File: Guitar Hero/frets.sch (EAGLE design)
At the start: 9 parts

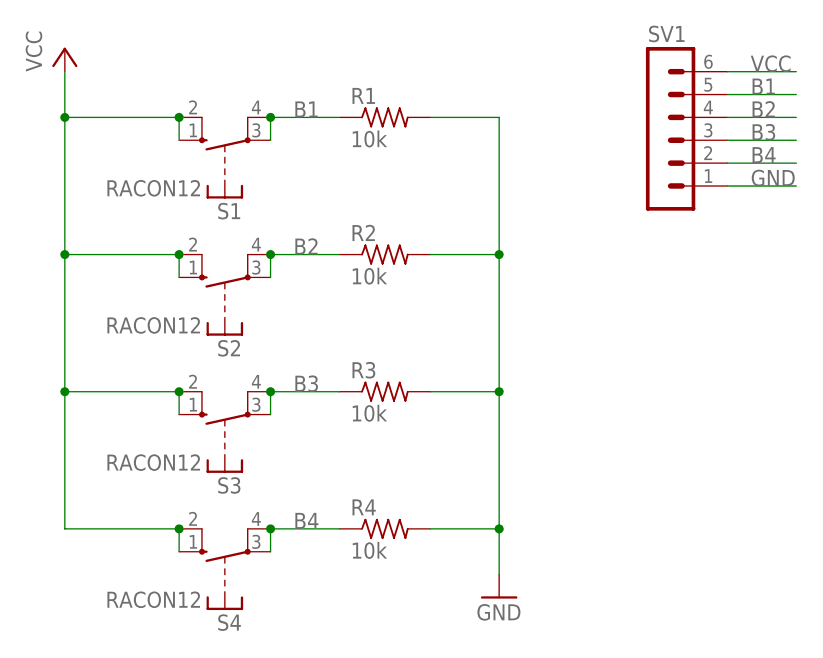
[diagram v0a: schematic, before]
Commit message: Started on base board; made board layout for peripherals
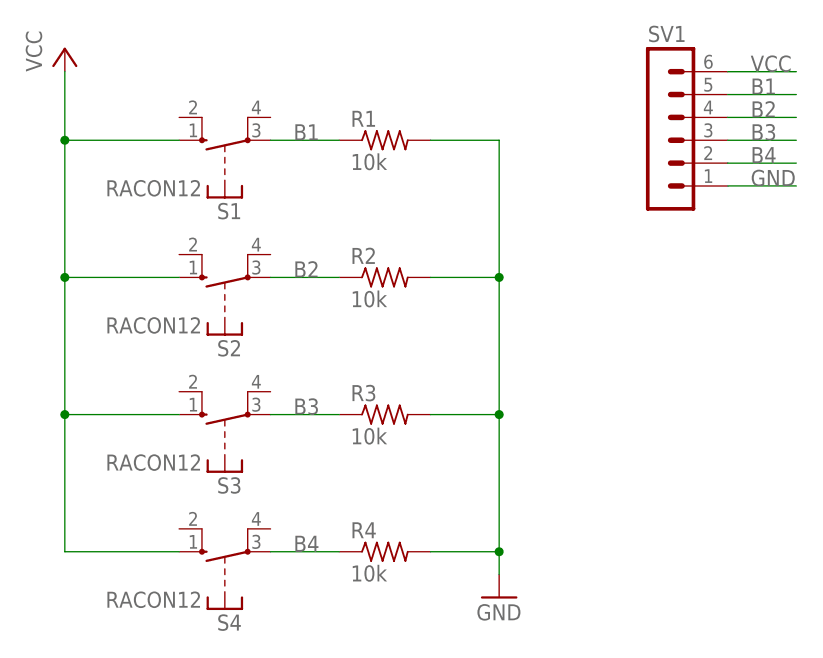
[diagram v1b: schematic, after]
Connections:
- net B1: no longer S1.P@1
- net B2: no longer S2.P@1
- net B3: no longer S3.P@1
- net B4: no longer S4.P@1
- net VCC: no longer S1.S@1, S2.S@1, S3.S@1, S4.S@1
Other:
- moved on the sheet: R1, R2, R3, R4
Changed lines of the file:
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@@
 </plain>
 <instances>
-<instance part="R1" gate="G$1" x="38.1" y="76.2"/>
-<instance part="R2" gate="G$1" x="38.1" y="60.96"/>
-<instance part="R3" gate="G$1" x="38.1" y="45.72"/>
-<instance part="R4" gate="G$1" x="38.1" y="30.48"/>
+<instance part="R1" gate="G$1" x="38.1" y="73.66"/>
+<instance part="R2" gate="G$1" x="38.1" y="58.42"/>
+<instance part="R3" gate="G$1" x="38.1" y="43.18"/>
+<instance part="R4" gate="G$1" x="38.1" y="27.94"/>
 <instance part="S1" gate="1" x="20.32" y="73.66" rot="R90"/>
 <instance part="S2" gate="1" x="20.32" y="58.42" rot="R90"/>
@@
 <net name="B1" class="0">
 <segment>
-<pinref part="S1" gate="1" pin="P@1"/>
 <pinref part="R1" gate="G$1" pin="1"/>
-<wire x1="25.4" y1="76.2" x2="33.02" y2="76.2" width="0.1524" layer="91"/>
-<label x="27.94" y="76.2" size="1.778" layer="95"/>
+<label x="27.94" y="73.66" size="1.778" layer="95"/>
 <pinref part="S1" gate="1" pin="P"/>
-<wire x1="25.4" y1="73.66" x2="25.4" y2="76.2" width="0.1524" layer="91"/>
-<junction x="25.4" y="76.2"/>
+<wire x1="25.4" y1="73.66" x2="33.02" y2="73.66" width="0.1524" layer="91"/>
 </segment>
 <segment>
@@
 <segment>
 <pinref part="R2" gate="G$1" pin="1"/>
-<pinref part="S2" gate="1" pin="P@1"/>
-<wire x1="33.02" y1="60.96" x2="25.4" y2="60.96" width="0.1524" layer="91"/>
-<label x="27.94" y="60.96" size="1.778" layer="95"/>
+<label x="27.94" y="58.42" size="1.778" layer="95"/>
 <pinref part="S2" gate="1" pin="P"/>
-<wire x1="25.4" y1="60.96" x2="25.4" y2="58.42" width="0.1524" layer="91"/>
-<junction x="25.4" y="60.96"/>
+<wire x1="33.02" y1="58.42" x2="25.4" y2="58.42" width="0.1524" layer="91"/>
 </segment>
 <segment>
@@
 <net name="B3" class="0">
 <segment>
-<pinref part="S3" gate="1" pin="P@1"/>
 <pinref part="R3" gate="G$1" pin="1"/>
-<wire x1="25.4" y1="45.72" x2="33.02" y2="45.72" width="0.1524" layer="91"/>
-<label x="27.94" y="45.72" size="1.778" layer="95"/>
+<label x="27.94" y="43.18" size="1.778" layer="95"/>
 <pinref part="S3" gate="1" pin="P"/>
-<wire x1="25.4" y1="43.18" x2="25.4" y2="45.72" width="0.1524" layer="91"/>
-<junction x="25.4" y="45.72"/>
+<wire x1="25.4" y1="43.18" x2="33.02" y2="43.18" width="0.1524" layer="91"/>
 </segment>
 <segment>
@@
 <net name="B4" class="0">
 <segment>
-<pinref part="S4" gate="1" pin="P@1"/>
 <pinref part="R4" gate="G$1" pin="1"/>
-<wire x1="25.4" y1="30.48" x2="33.02" y2="30.48" width="0.1524" layer="91"/>
-<label x="27.94" y="30.48" size="1.778" layer="95"/>
+<label x="27.94" y="27.94" size="1.778" layer="95"/>
 <pinref part="S4" gate="1" pin="P"/>
-<wire x1="25.4" y1="27.94" x2="25.4" y2="30.48" width="0.1524" layer="91"/>
-<junction x="25.4" y="30.48"/>
+<wire x1="33.02" y1="27.94" x2="25.4" y2="27.94" width="0.1524" layer="91"/>
 </segment>
 <segment>
@@
 <net name="VCC" class="0">
 <segment>
-<pinref part="S1" gate="1" pin="S@1"/>
-<wire x1="15.24" y1="76.2" x2="2.54" y2="76.2" width="0.1524" layer="91"/>
-<wire x1="2.54" y1="76.2" x2="2.54" y2="60.96" width="0.1524" layer="91"/>
-<pinref part="S4" gate="1" pin="S@1"/>
-<wire x1="2.54" y1="60.96" x2="2.54" y2="45.72" width="0.1524" layer="91"/>
-<wire x1="2.54" y1="45.72" x2="2.54" y2="30.48" width="0.1524" layer="91"/>
-<wire x1="2.54" y1="30.48" x2="15.24" y2="30.48" width="0.1524" layer="91"/>
-<pinref part="S3" gate="1" pin="S@1"/>
-<wire x1="15.24" y1="45.72" x2="2.54" y2="45.72" width="0.1524" layer="91"/>
-<junction x="2.54" y="45.72"/>
-<pinref part="S2" gate="1" pin="S@1"/>
-<wire x1="15.24" y1="60.96" x2="2.54" y2="60.96" width="0.1524" layer="91"/>
-<junction x="2.54" y="60.96"/>
+<wire x1="2.54" y1="81.28" x2="2.54" y2="73.66" width="0.1524" layer="91"/>
+<wire x1="2.54" y1="73.66" x2="2.54" y2="58.42" width="0.1524" layer="91"/>
+<wire x1="2.54" y1="58.42" x2="2.54" y2="43.18" width="0.1524" layer="91"/>
+<wire x1="2.54" y1="43.18" x2="2.54" y2="27.94" width="0.1524" layer="91"/>
 <pinref part="P+1" gate="VCC" pin="VCC"/>
-<wire x1="2.54" y1="81.28" x2="2.54" y2="76.2" width="0.1524" layer="91"/>
-<junction x="2.54" y="76.2"/>
+<pinref part="S4" gate="1" pin="S"/>
 <pinref part="S1" gate="1" pin="S"/>
-<wire x1="15.24" y1="73.66" x2="15.24" y2="76.2" width="0.1524" layer="91"/>
-<junction x="15.24" y="76.2"/>
+<wire x1="15.24" y1="73.66" x2="2.54" y2="73.66" width="0.1524" layer="91"/>
+<junction x="2.54" y="73.66"/>
 <pinref part="S2" gate="1" pin="S"/>
-<wire x1="15.24" y1="60.96" x2="15.24" y2="58.42" width="0.1524" layer="91"/>
-<junction x="15.24" y="60.96"/>
+<wire x1="15.24" y1="58.42" x2="2.54" y2="58.42" width="0.1524" layer="91"/>
+<junction x="2.54" y="58.42"/>
 <pinref part="S3" gate="1" pin="S"/>
-<wire x1="15.24" y1="43.18" x2="15.24" y2="45.72" width="0.1524" layer="91"/>
-<junction x="15.24" y="45.72"/>
-<pinref part="S4" gate="1" pin="S"/>
-<wire x1="15.24" y1="27.94" x2="15.24" y2="30.48" width="0.1524" layer="91"/>
-<junction x="15.24" y="30.48"/>
+<wire x1="15.24" y1="43.18" x2="2.54" y2="43.18" width="0.1524" layer="91"/>
+<junction x="2.54" y="43.18"/>
+<wire x1="15.24" y1="27.94" x2="2.54" y2="27.94" width="0.1524" layer="91"/>
 </segment>
 <segment>
@@
 <segment>
 <pinref part="R1" gate="G$1" pin="2"/>
-<wire x1="43.18" y1="76.2" x2="50.8" y2="76.2" width="0.1524" layer="91"/>
-<wire x1="50.8" y1="76.2" x2="50.8" y2="60.96" width="0.1524" layer="91"/>
+<wire x1="43.18" y1="73.66" x2="50.8" y2="73.66" width="0.1524" layer="91"/>
+<wire x1="50.8" y1="73.66" x2="50.8" y2="58.42" width="0.1524" layer="91"/>
 <pinref part="R4" gate="G$1" pin="2"/>
-<wire x1="50.8" y1="60.96" x2="50.8" y2="45.72" width="0.1524" layer="91"/>
-<wire x1="50.8" y1="45.72" x2="50.8" y2="30.48" width="0.1524" layer="91"/>
-<wire x1="50.8" y1="30.48" x2="43.18" y2="30.48" width="0.1524" layer="91"/>
+<wire x1="50.8" y1="58.42" x2="50.8" y2="43.18" width="0.1524" layer="91"/>
+<wire x1="50.8" y1="43.18" x2="50.8" y2="27.94" width="0.1524" layer="91"/>
+<wire x1="50.8" y1="27.94" x2="43.18" y2="27.94" width="0.1524" layer="91"/>
 <pinref part="R3" gate="G$1" pin="2"/>
-<wire x1="43.18" y1="45.72" x2="50.8" y2="45.72" width="0.1524" layer="91"/>
-<junction x="50.8" y="45.72"/>
+<wire x1="43.18" y1="43.18" x2="50.8" y2="43.18" width="0.1524" layer="91"/>
+<junction x="50.8" y="43.18"/>
 <pinref part="R2" gate="G$1" pin="2"/>
-<wire x1="43.18" y1="60.96" x2="50.8" y2="60.96" width="0.1524" layer="91"/>
-<junction x="50.8" y="60.96"/>
+<wire x1="43.18" y1="58.42" x2="50.8" y2="58.42" width="0.1524" layer="91"/>
+<junction x="50.8" y="58.42"/>
 <pinref part="GND1" gate="1" pin="GND"/>
-<wire x1="50.8" y1="25.4" x2="50.8" y2="30.48" width="0.1524" layer="91"/>
-<junction x="50.8" y="30.48"/>
+<wire x1="50.8" y1="25.4" x2="50.8" y2="27.94" width="0.1524" layer="91"/>
+<junction x="50.8" y="27.94"/>
 </segment>
 <segment>
